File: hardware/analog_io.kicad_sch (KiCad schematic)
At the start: 40 parts, among them J24 AI0/GND/AI1/GND/AI2, J25 0-10 V outputs 0-3; pin 1 = c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, U37 L78L12ACUTR, U38 TLV2374IDR

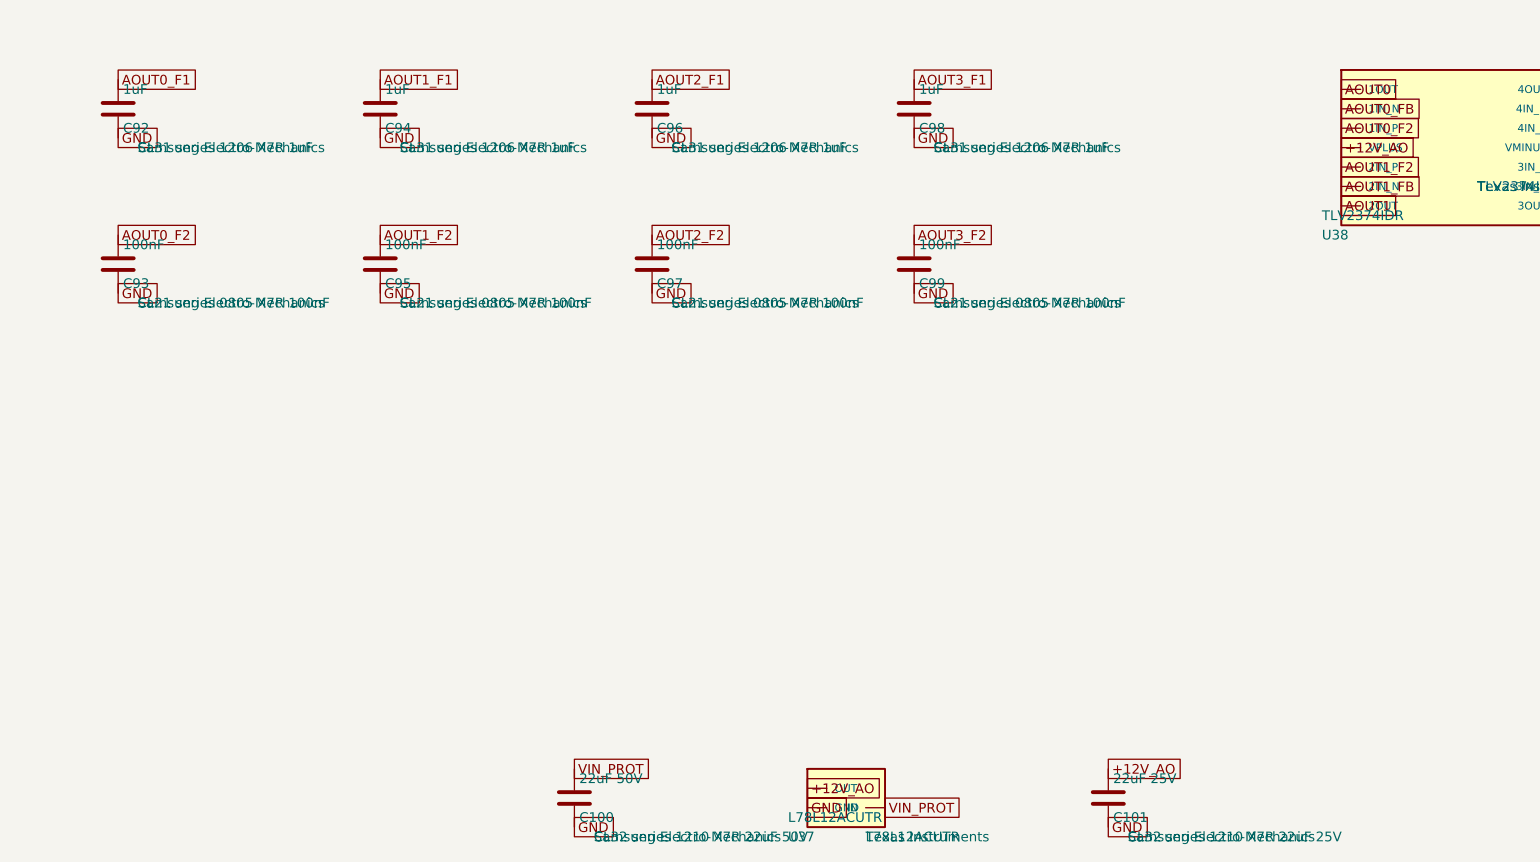
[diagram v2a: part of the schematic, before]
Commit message: Standardize passives and add microSD alternate
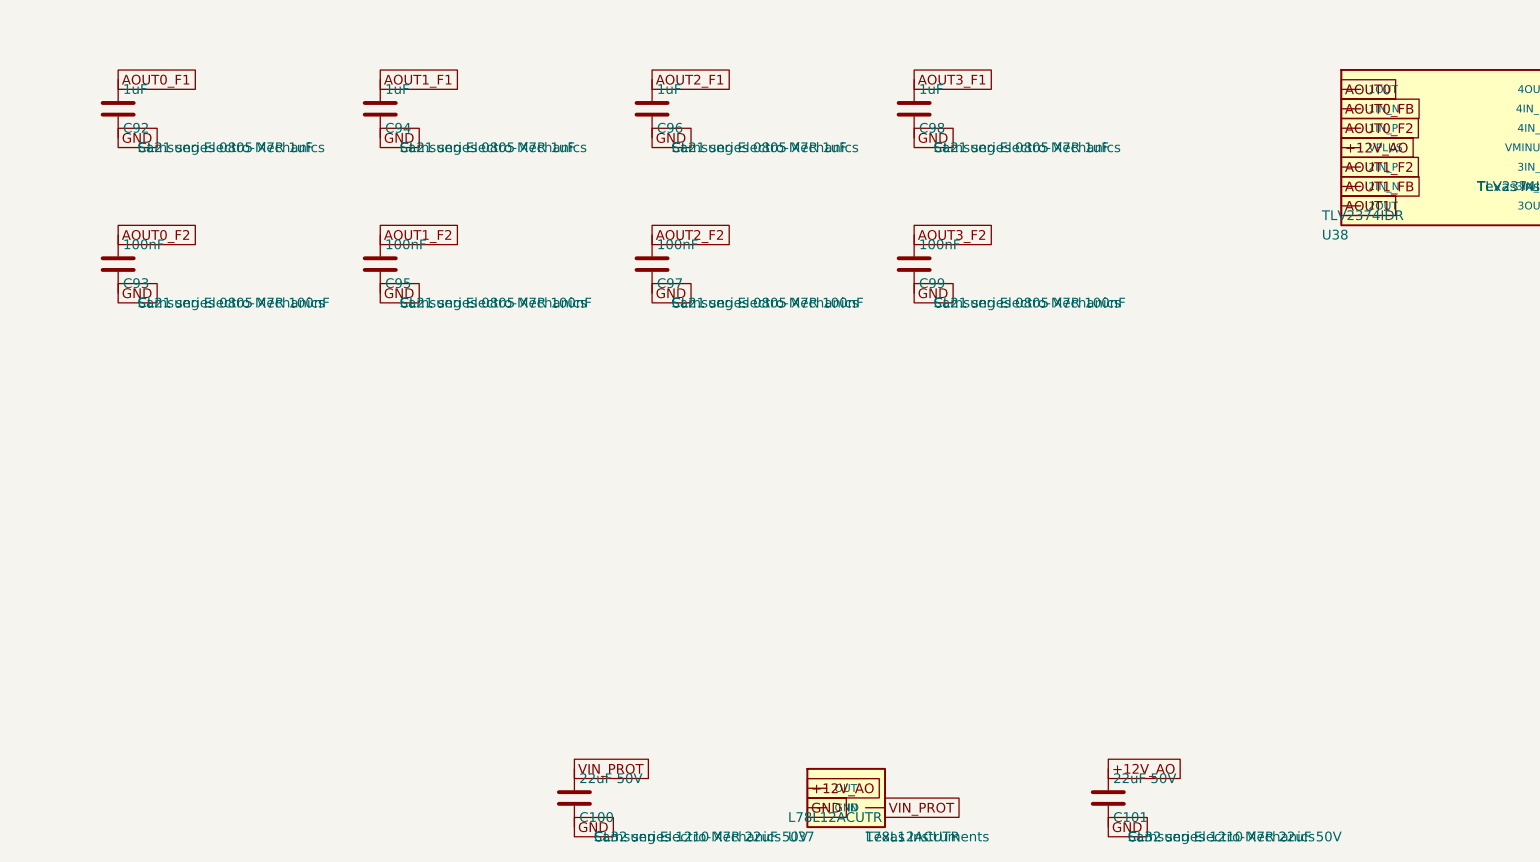
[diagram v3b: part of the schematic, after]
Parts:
- C101: value 22uF 25V -> 22uF 50V; MPN CL32 series 1210 X7R 22uF 25V -> CL32 series 1210 X7R 22uF 50V
- C92, C94, C96, C98: footprint Capacitor_SMD:C_1206_3216Metric -> Capacitor_SMD:C_0805_2012Metric; MPN CL31 series 1206 X7R 1uF -> CL21 series 0805 X7R 1uF
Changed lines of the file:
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@@
 		(instances
 			(project "Analog I/O"
-				(path "/7556d853-629e-4a43-b2a7-51d3b1a45efc"
+				(path "/34b0f4bf-46a7-47f0-aca1-10aec9cc9676"
 					(reference "J24")
 					(unit 1)
@@
 		(instances
 			(project "Analog I/O"
-				(path "/7556d853-629e-4a43-b2a7-51d3b1a45efc"
+				(path "/34b0f4bf-46a7-47f0-aca1-10aec9cc9676"
 					(reference "R61")
 					(unit 1)
@@
 		(instances
 			(project "Analog I/O"
-				(path "/7556d853-629e-4a43-b2a7-51d3b1a45efc"
+				(path "/34b0f4bf-46a7-47f0-aca1-10aec9cc9676"
 					(reference "R63")
 					(unit 1)
@@
 		(instances
 			(project "Analog I/O"
-				(path "/7556d853-629e-4a43-b2a7-51d3b1a45efc"
+				(path "/34b0f4bf-46a7-47f0-aca1-10aec9cc9676"
 					(reference "C73")
 					(unit 1)
@@
 		(instances
 			(project "Analog I/O"
-				(path "/7556d853-629e-4a43-b2a7-51d3b1a45efc"
+				(path "/34b0f4bf-46a7-47f0-aca1-10aec9cc9676"
 					(reference "R64")
 					(unit 1)
@@
 		(instances
 			(project "Analog I/O"
-				(path "/7556d853-629e-4a43-b2a7-51d3b1a45efc"
+				(path "/34b0f4bf-46a7-47f0-aca1-10aec9cc9676"
 					(reference "R66")
 					(unit 1)
@@
 		(instances
 			(project "Analog I/O"
-				(path "/7556d853-629e-4a43-b2a7-51d3b1a45efc"
+				(path "/34b0f4bf-46a7-47f0-aca1-10aec9cc9676"
 					(reference "C74")
 					(unit 1)
@@
 		(instances
 			(project "Analog I/O"
-				(path "/7556d853-629e-4a43-b2a7-51d3b1a45efc"
+				(path "/34b0f4bf-46a7-47f0-aca1-10aec9cc9676"
 					(reference "R67")
 					(unit 1)
@@
 		(instances
 			(project "Analog I/O"
-				(path "/7556d853-629e-4a43-b2a7-51d3b1a45efc"
+				(path "/34b0f4bf-46a7-47f0-aca1-10aec9cc9676"
 					(reference "R69")
 					(unit 1)
@@
 		(instances
 			(project "Analog I/O"
-				(path "/7556d853-629e-4a43-b2a7-51d3b1a45efc"
+				(path "/34b0f4bf-46a7-47f0-aca1-10aec9cc9676"
 					(reference "C75")
 					(unit 1)
@@
 		(instances
 			(project "Analog I/O"
-				(path "/7556d853-629e-4a43-b2a7-51d3b1a45efc"
+				(path "/34b0f4bf-46a7-47f0-aca1-10aec9cc9676"
 					(reference "J25")
 					(unit 1)
@@
 		(instances
 			(project "Analog I/O"
-				(path "/7556d853-629e-4a43-b2a7-51d3b1a45efc"
+				(path "/34b0f4bf-46a7-47f0-aca1-10aec9cc9676"
 					(reference "R92")
 					(unit 1)
@@
 		(instances
 			(project "Analog I/O"
-				(path "/7556d853-629e-4a43-b2a7-51d3b1a45efc"
+				(path "/34b0f4bf-46a7-47f0-aca1-10aec9cc9676"
 					(reference "R96")
 					(unit 1)
@@
 		(instances
 			(project "Analog I/O"
-				(path "/7556d853-629e-4a43-b2a7-51d3b1a45efc"
+				(path "/34b0f4bf-46a7-47f0-aca1-10aec9cc9676"
 					(reference "R100")
 					(unit 1)
@@
 		(instances
 			(project "Analog I/O"
-				(path "/7556d853-629e-4a43-b2a7-51d3b1a45efc"
+				(path "/34b0f4bf-46a7-47f0-aca1-10aec9cc9676"
 					(reference "R104")
 					(unit 1)
@@
 		(instances
 			(project "Analog I/O"
-				(path "/7556d853-629e-4a43-b2a7-51d3b1a45efc"
+				(path "/34b0f4bf-46a7-47f0-aca1-10aec9cc9676"
 					(reference "R93")
 					(unit 1)
@@
 		(instances
 			(project "Analog I/O"
-				(path "/7556d853-629e-4a43-b2a7-51d3b1a45efc"
+				(path "/34b0f4bf-46a7-47f0-aca1-10aec9cc9676"
 					(reference "R97")
 					(unit 1)
@@
 		(instances
 			(project "Analog I/O"
-				(path "/7556d853-629e-4a43-b2a7-51d3b1a45efc"
+				(path "/34b0f4bf-46a7-47f0-aca1-10aec9cc9676"
 					(reference "R101")
 					(unit 1)
@@
 		(instances
 			(project "Analog I/O"
-				(path "/7556d853-629e-4a43-b2a7-51d3b1a45efc"
+				(path "/34b0f4bf-46a7-47f0-aca1-10aec9cc9676"
 					(reference "R105")
 					(unit 1)
@@
 		(instances
 			(project "Analog I/O"
-				(path "/7556d853-629e-4a43-b2a7-51d3b1a45efc"
+				(path "/34b0f4bf-46a7-47f0-aca1-10aec9cc9676"
 					(reference "R94")
 					(unit 1)
@@
 		(instances
 			(project "Analog I/O"
-				(path "/7556d853-629e-4a43-b2a7-51d3b1a45efc"
+				(path "/34b0f4bf-46a7-47f0-aca1-10aec9cc9676"
 					(reference "R98")
 					(unit 1)
@@
 		(instances
 			(project "Analog I/O"
-				(path "/7556d853-629e-4a43-b2a7-51d3b1a45efc"
+				(path "/34b0f4bf-46a7-47f0-aca1-10aec9cc9676"
 					(reference "R102")
 					(unit 1)
@@
 		(instances
 			(project "Analog I/O"
-				(path "/7556d853-629e-4a43-b2a7-51d3b1a45efc"
+				(path "/34b0f4bf-46a7-47f0-aca1-10aec9cc9676"
 					(reference "R106")
 					(unit 1)
@@
 		(instances
 			(project "Analog I/O"
-				(path "/7556d853-629e-4a43-b2a7-51d3b1a45efc"
+				(path "/34b0f4bf-46a7-47f0-aca1-10aec9cc9676"
 					(reference "R95")
 					(unit 1)
@@
 		(instances
 			(project "Analog I/O"
-				(path "/7556d853-629e-4a43-b2a7-51d3b1a45efc"
+				(path "/34b0f4bf-46a7-47f0-aca1-10aec9cc9676"
 					(reference "R99")
 					(unit 1)
@@
 		(instances
 			(project "Analog I/O"
-				(path "/7556d853-629e-4a43-b2a7-51d3b1a45efc"
+				(path "/34b0f4bf-46a7-47f0-aca1-10aec9cc9676"
 					(reference "R103")
 					(unit 1)
@@
 		(instances
 			(project "Analog I/O"
-				(path "/7556d853-629e-4a43-b2a7-51d3b1a45efc"
+				(path "/34b0f4bf-46a7-47f0-aca1-10aec9cc9676"
 					(reference "R107")
 					(unit 1)
@@
 			)
 		)
-		(property "Footprint" "Capacitor_SMD:C_1206_3216Metric"
+		(property "Footprint" "Capacitor_SMD:C_0805_2012Metric"
 			(at 256.2352 200.66 0.0000)
 			(effects
@@
 			)
 		)
-		(property "MPN" "CL31 series 1206 X7R 1uF"
+		(property "MPN" "CL21 series 0805 X7R 1uF"
 			(at 257.81 209.5499 0)
 			(effects
@@
 		(instances
 			(project "Analog I/O"
-				(path "/7556d853-629e-4a43-b2a7-51d3b1a45efc"
+				(path "/34b0f4bf-46a7-47f0-aca1-10aec9cc9676"
 					(reference "C92")
 					(unit 1)
@@
 		(instances
 			(project "Analog I/O"
-				(path "/7556d853-629e-4a43-b2a7-51d3b1a45efc"
+				(path "/34b0f4bf-46a7-47f0-aca1-10aec9cc9676"
 					(reference "C93")
 					(unit 1)
@@
 			)
 		)
-		(property "Footprint" "Capacitor_SMD:C_1206_3216Metric"
+		(property "Footprint" "Capacitor_SMD:C_0805_2012Metric"
 			(at 290.5252 200.66 0.0000)
 			(effects
@@
 			)
 		)
-		(property "MPN" "CL31 series 1206 X7R 1uF"
+		(property "MPN" "CL21 series 0805 X7R 1uF"
 			(at 292.1 209.5499 0)
 			(effects
@@
 		(instances
 			(project "Analog I/O"
-				(path "/7556d853-629e-4a43-b2a7-51d3b1a45efc"
+				(path "/34b0f4bf-46a7-47f0-aca1-10aec9cc9676"
 					(reference "C94")
 					(unit 1)
@@
 		(instances
 			(project "Analog I/O"
-				(path "/7556d853-629e-4a43-b2a7-51d3b1a45efc"
+				(path "/34b0f4bf-46a7-47f0-aca1-10aec9cc9676"
 					(reference "C95")
 					(unit 1)
@@
 			)
 		)
-		(property "Footprint" "Capacitor_SMD:C_1206_3216Metric"
+		(property "Footprint" "Capacitor_SMD:C_0805_2012Metric"
 			(at 326.0852 200.66 0.0000)
 			(effects
@@
 			)
 		)
-		(property "MPN" "CL31 series 1206 X7R 1uF"
+		(property "MPN" "CL21 series 0805 X7R 1uF"
 			(at 327.66 209.5499 0)
 			(effects
@@
 		(instances
 			(project "Analog I/O"
-				(path "/7556d853-629e-4a43-b2a7-51d3b1a45efc"
+				(path "/34b0f4bf-46a7-47f0-aca1-10aec9cc9676"
 					(reference "C96")
 					(unit 1)
@@
 		(instances
 			(project "Analog I/O"
-				(path "/7556d853-629e-4a43-b2a7-51d3b1a45efc"
+				(path "/34b0f4bf-46a7-47f0-aca1-10aec9cc9676"
 					(reference "C97")
 					(unit 1)
@@
 			)
 		)
-		(property "Footprint" "Capacitor_SMD:C_1206_3216Metric"
+		(property "Footprint" "Capacitor_SMD:C_0805_2012Metric"
 			(at 360.3752 200.66 0.0000)
 			(effects
@@
 			)
 		)
-		(property "MPN" "CL31 series 1206 X7R 1uF"
+		(property "MPN" "CL21 series 0805 X7R 1uF"
 			(at 361.95 209.5499 0)
 			(effects
@@
 		(instances
 			(project "Analog I/O"
-				(path "/7556d853-629e-4a43-b2a7-51d3b1a45efc"
+				(path "/34b0f4bf-46a7-47f0-aca1-10aec9cc9676"
 					(reference "C98")
 					(unit 1)
@@
 		(instances
 			(project "Analog I/O"
-				(path "/7556d853-629e-4a43-b2a7-51d3b1a45efc"
+				(path "/34b0f4bf-46a7-47f0-aca1-10aec9cc9676"
 					(reference "C99")
 					(unit 1)
@@
 		(instances
 			(project "Analog I/O"
-				(path "/7556d853-629e-4a43-b2a7-51d3b1a45efc"
+				(path "/34b0f4bf-46a7-47f0-aca1-10aec9cc9676"
 					(reference "U38")
 					(unit 1)
@@
 		(instances
 			(project "Analog I/O"
-				(path "/7556d853-629e-4a43-b2a7-51d3b1a45efc"
+				(path "/34b0f4bf-46a7-47f0-aca1-10aec9cc9676"
 					(reference "U37")
 					(unit 1)
@@
 		(instances
 			(project "Analog I/O"
-				(path "/7556d853-629e-4a43-b2a7-51d3b1a45efc"
+				(path "/34b0f4bf-46a7-47f0-aca1-10aec9cc9676"
 					(reference "C100")
 					(unit 1)
@@
 			)
 		)
-		(property "Value" "22uF 25V"
+		(property "Value" "22uF 50V"
 			(at 385.445 292.1 0.0000)
 			(effects
@@
 			)
 		)
-		(property "MPN" "CL32 series 1210 X7R 22uF 25V"
+		(property "MPN" "CL32 series 1210 X7R 22uF 50V"
 			(at 387.35 299.7199 0)
 			(effects
@@
 		(instances
 			(project "Analog I/O"
-				(path "/7556d853-629e-4a43-b2a7-51d3b1a45efc"
+				(path "/34b0f4bf-46a7-47f0-aca1-10aec9cc9676"
 					(reference "C101")
 					(unit 1)
@@
 		(instances
 			(project "Analog I/O"
-				(path "/7556d853-629e-4a43-b2a7-51d3b1a45efc"
+				(path "/34b0f4bf-46a7-47f0-aca1-10aec9cc9676"
 					(reference "C102")
 					(unit 1)
